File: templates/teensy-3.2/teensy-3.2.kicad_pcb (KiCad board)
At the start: 2 copper layers, 1 part, among them J1 TEENSY3.2-72MHz

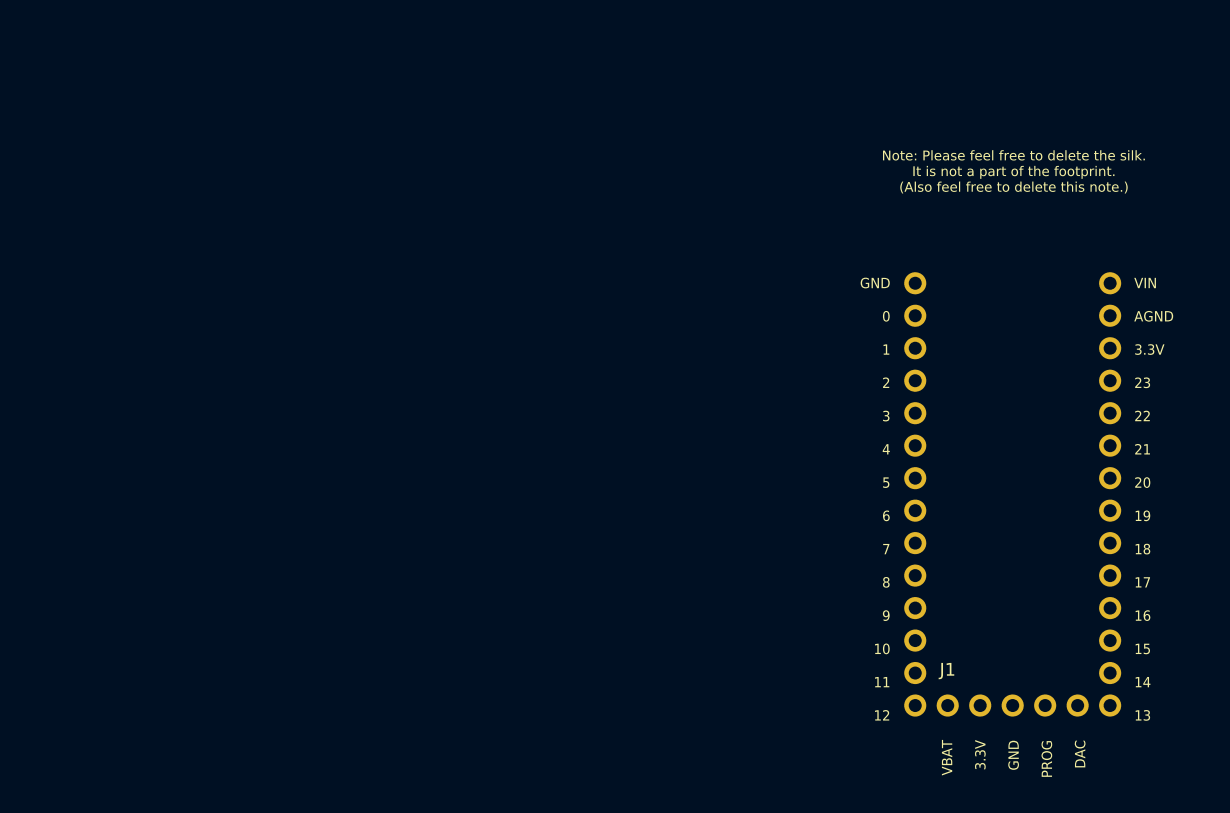
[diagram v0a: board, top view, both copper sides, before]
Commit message: Add fab notes to Dwgs.User
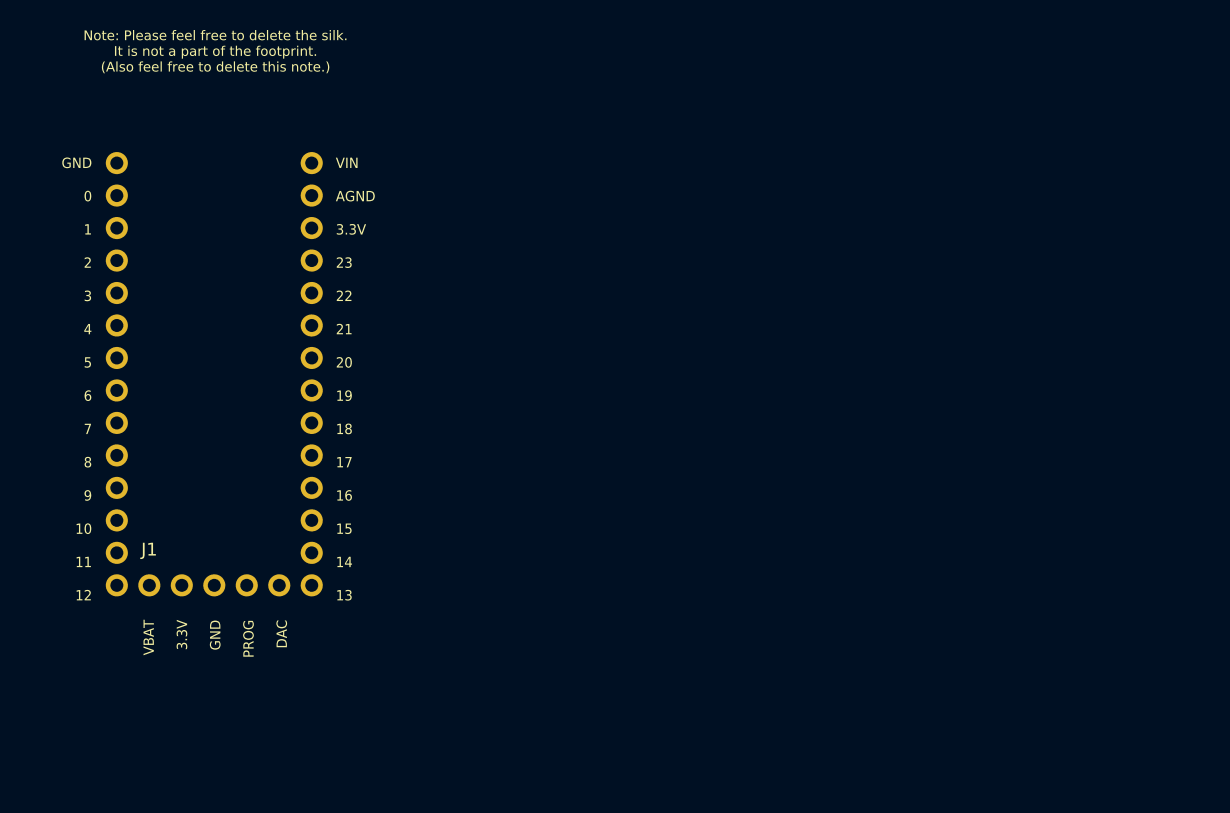
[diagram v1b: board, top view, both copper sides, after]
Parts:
- moved J1 63.1 mm to (40.0, 78.6)
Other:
- board text added: "FABRICATION NOTES 1. THIS IS A 2 LAYER BOARD. 2. EXTERNAL LAYERS SHALL HAVE 1 OZ COPPER. 3. MATERIAL: FR4 AND 0.062 INCH +/- 10% THICK. 4. BOARDS SHALL BE ROHS COMPLIANT. 5. MANUFACTURE IN ACCORDANCE WITH IPC-6012 CLASS 2 6. MASK: BOTH SIDES OF THE BOARD SHALL HAVE SOLDER MASK (ANY COLOR) OVER BARE COPPER. 7. SILK: BOTH SIDES OF THE BOARD SHALL HAVE WHITE SILKSCREEN. DO NOT PLACE SILK OVER BARE C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"
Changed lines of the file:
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@@
-(kicad_pcb (version 4) (host pcbnew 4.0.5-e0-6337~49~ubuntu16.04.1)
+(kicad_pcb (version 4) (host pcbnew 4.0.7-e2-6376~58~ubuntu16.04.1)
   (general
-    (links 0)
+    (links 3)
     (no_connects 3)
     (area 90.895714 61.595 178.510001 123.265001)
     (thickness 1.6)
-    (drawings 21)
+    (drawings 5)
     (tracks 0)
     (zones 0)
@@
     (38 B.Mask user)
     (39 F.Mask user)
+    (40 Dwgs.User user)
     (44 Edge.Cuts user)
     (46 B.CrtYd user)
@@
   )
   (module Wickerlib:TEENSY-3.2-NOSILK (layer F.Cu)
-    (at 102.3874 87.9856)
+    (at 39.9542 78.5876)
     (fp_text reference J1 (at 0 -0.127) (layer F.Fab)
       (effects (font (size 1 1) (thickness 0.15)))
@@
     (pad 15 thru_hole circle (at 8.001 12.192) (size 1.7272 1.7272) (drill 1.016) (layers *.Cu *.Mask F.SilkS))
   )
-  (gr_text "Note: Please feel free to delete the silk.\nIt is not a part of the footprint.\n(Also feel free to delete this note.)" (at 102.87 63.5) (layer F.SilkS)
+  (gr_text "FABRICATION NOTES\n\n1. THIS IS A 2 LAYER BOARD. \n2. EXTERNAL LAYERS SHALL HAVE 1 OZ COPPER.\n3. MATERIAL: FR4 AND 0.062 INCH +/- 10% THICK.\n4. BOARDS SHALL BE ROHS COMPLIANT. \n5. MANUFACTURE IN ACCORDANCE WITH IPC-6012 CLASS 2\n6. MASK: BOTH SIDES OF THE BOARD SHALL HAVE \n   SOLDER MASK (ANY COLOR) OVER BARE COPPER. \n7. SILK: BOTH SIDES OF THE BOARD SHALL HAVE \n   WHITE SILKSCREEN. DO NOT PLACE SILK OVER BARE COPPER.\n8. FINISH: ENIG.\n9. MINIMUM TRACE WIDTH - 0.006 INCH.\n   MINIMUM SPACE - 0.006 INCH.\n   MINIMUM HOLE DIA - 0.013 INCH. \n10. MAX HOLE PLACEMENT TOLERANCE OF +/- 0.003 INCH.\n11. MAX HOLE DIAMETER TOLERANCE OF +/- 0.003 INCH AFTER PLATING." (at 75.184 85.4964) (layer Dwgs.User)
+    (effects (font (size 2.54 2.54) (thickness 0.254)) (justify left))
+  )
+  (gr_text "Note: Please feel free to delete the silk.\nIt is not a part of the footprint.\n(Also feel free to delete this note.)" (at 40.4368 54.102) (layer F.SilkS)
     (effects (font (size 0.762 0.762) (thickness 0.1524)))
   )
-  (gr_text "VIN\n\nAGND\n\n3.3V\n\n23\n\n22\n\n21\n\n20\n\n19\n\n18\n\n17\n\n16\n\n15\n\n14\n\n13\n" (at 112.268 89.154) (layer F.SilkS)
+  (gr_text "VIN\n\nAGND\n\n3.3V\n\n23\n\n22\n\n21\n\n20\n\n19\n\n18\n\n17\n\n16\n\n15\n\n14\n\n13\n" (at 49.8348 79.756) (layer F.SilkS)
     (effects (font (size 0.80772 0.762) (thickness 0.1524)) (justify left))
   )
-  (gr_text "GND\n\n0\n\n1\n\n2\n\n3\n\n4\n\n5\n\n6\n\n7\n\n8\n\n9\n\n10\n\n11\n\n12" (at 93.218 89.154) (layer F.SilkS)
+  (gr_text "GND\n\n0\n\n1\n\n2\n\n3\n\n4\n\n5\n\n6\n\n7\n\n8\n\n9\n\n10\n\n11\n\n12" (at 30.7848 79.756) (layer F.SilkS)
     (effects (font (size 0.80772 0.762) (thickness 0.1524)) (justify right))
   )
-  (gr_text "VBAT\n\n3.3V\n\nGND\n\nPROG\n\nDAC" (at 102.87 107.95 90) (layer F.SilkS)
+  (gr_text "VBAT\n\n3.3V\n\nGND\n\nPROG\n\nDAC" (at 40.4368 98.552 90) (layer F.SilkS)
     (effects (font (size 0.80772 0.762) (thickness 0.1524)) (justify right))
   )
-  (gr_circle (center 117.348 76.962) (end 118.618 76.962) (layer Dwgs.User) (width 0.15))
-  (gr_line (start 114.427 78.994) (end 114.427 74.93) (angle 90) (layer Dwgs.User) (width 0.15))
-  (gr_line (start 120.269 78.994) (end 114.427 78.994) (angle 90) (layer Dwgs.User) (width 0.15))
-  (gr_line (start 120.269 74.93) (end 120.269 78.994) (angle 90) (layer Dwgs.User) (width 0.15))
-  (gr_line (start 114.427 74.93) (end 120.269 74.93) (angle 90) (layer Dwgs.User) (width 0.15))
-  (gr_line (start 120.523 93.98) (end 104.648 93.98) (angle 90) (layer Dwgs.User) (width 0.15))
-  (gr_line (start 173.355 102.235) (end 173.355 94.615) (angle 90) (layer Dwgs.User) (width 0.15))
-  (gr_line (start 178.435 102.235) (end 173.355 102.235) (angle 90) (layer Dwgs.User) (width 0.15))
-  (gr_line (start 178.435 94.615) (end 178.435 102.235) (angle 90) (layer Dwgs.User) (width 0.15))
-  (gr_line (start 173.355 94.615) (end 178.435 94.615) (angle 90) (layer Dwgs.User) (width 0.15))
-  (gr_line (start 109.093 123.19) (end 109.093 114.3) (angle 90) (layer Dwgs.User) (width 0.15))
-  (gr_line (start 122.428 123.19) (end 109.093 123.19) (angle 90) (layer Dwgs.User) (width 0.15))
-  (gr_line (start 122.428 114.3) (end 122.428 123.19) (angle 90) (layer Dwgs.User) (width 0.15))
-  (gr_line (start 109.093 114.3) (end 122.428 114.3) (angle 90) (layer Dwgs.User) (width 0.15))
-  (gr_line (start 104.648 93.98) (end 104.648 82.55) (angle 90) (layer Dwgs.User) (width 0.15))
-  (gr_line (start 120.523 82.55) (end 120.523 93.98) (angle 90) (layer Dwgs.User) (width 0.15))
-  (gr_line (start 104.648 82.55) (end 120.523 82.55) (angle 90) (layer Dwgs.User) (width 0.15))
 )
